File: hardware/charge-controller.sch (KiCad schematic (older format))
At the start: 47 parts, among them J1 Conn_02x04_Odd_Even, J2 Conn_02x03_Odd_Even, J4 CAN_TERM, Q1 MMBT3904, Q2 NCV8402xST, Q3 NCV8402xST, Q4 NCV8402xST, Q5 NCV8402xST, U1 Pico, U2 MCP2515-xST, U3 SN65HVD230, U4 TPS62160DGK

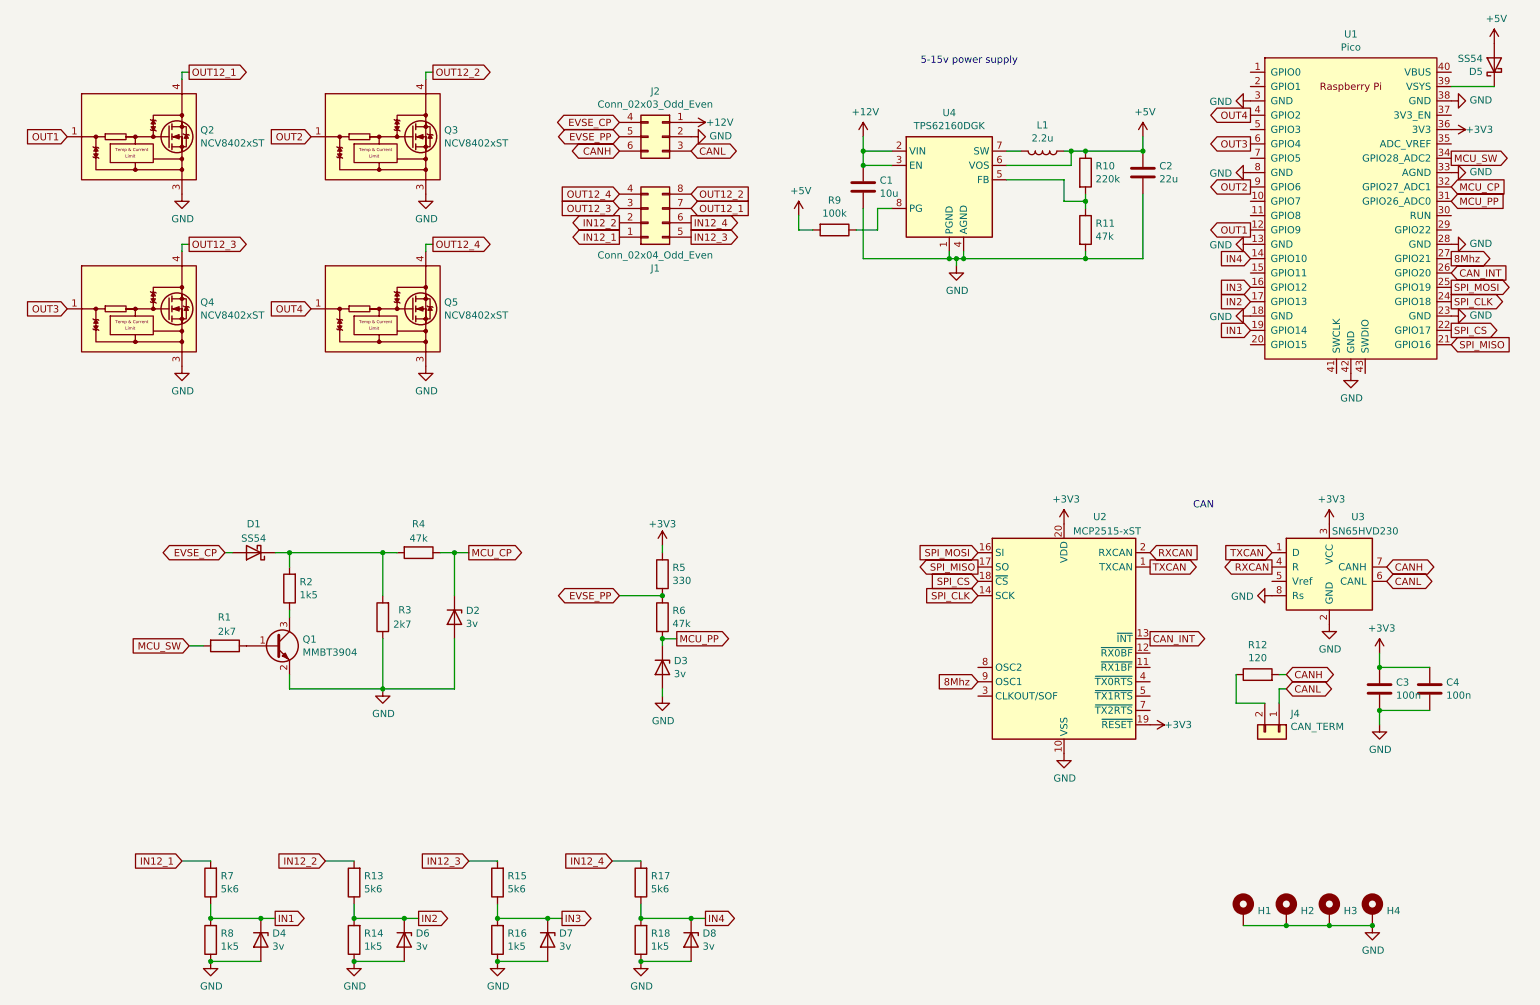
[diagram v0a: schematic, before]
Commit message: improve 12v inputs, connect CAN line driver sleep pin
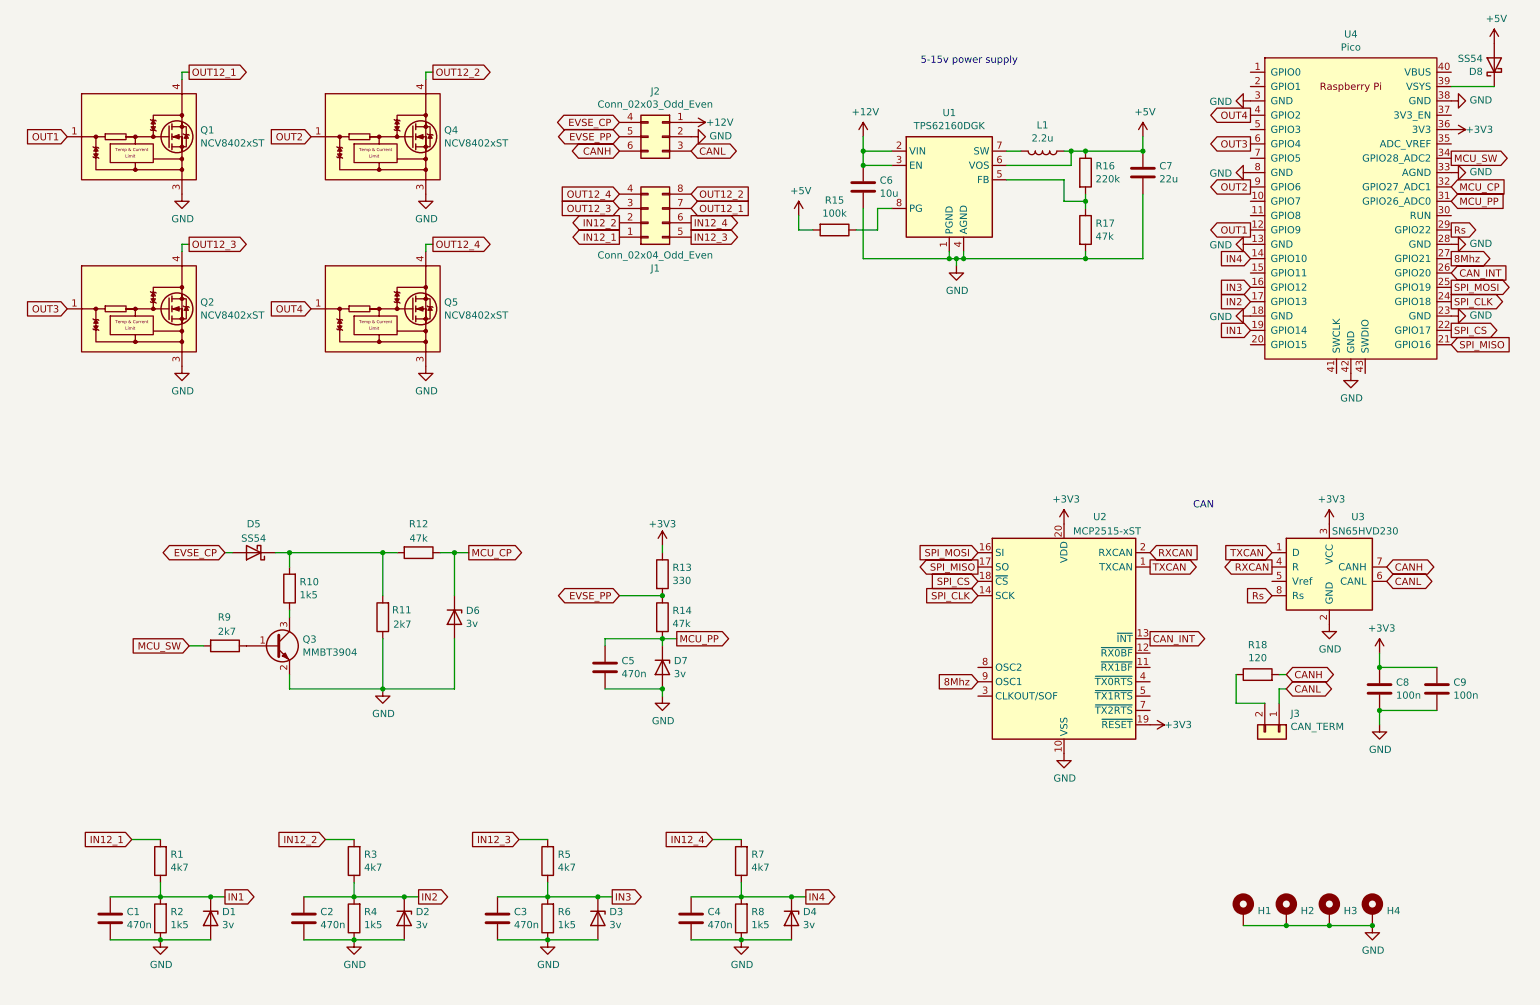
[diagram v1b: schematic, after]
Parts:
- added C1, C2, C3, C4, C5: 470n, Capacitor_SMD:C_0603_1608Metric, symbol Device:C
- R1: renamed from R7; value 5k6 -> 4k7; LCSC C23189 -> C23162
- R3: renamed from R13; value 5k6 -> 4k7; LCSC C23189 -> C23162
- R5: renamed from R15; value 5k6 -> 4k7; LCSC C23189 -> C23162
- R7: renamed from R17; value 5k6 -> 4k7; LCSC C23189 -> C23162
- renumbered C1 to C6, C2 to C7, C3 to C8, C4 to C9, D4 to D1, D6 to D2, D7 to D3, D8 to D4, D1 to D5, D2 to D6, D3 to D7, D5 to D8, J4 to J3, Q2 to Q1, Q4 to Q2, Q1 to Q3, Q3 to Q4, R2 to R10, R3 to R11, R4 to R12, R5 to R13, R6 to R14, R9 to R15, R10 to R16, R11 to R17, R12 to R18, R8 to R2, R14 to R4, R16 to R6, R18 to R8, R1 to R9, U4 to U1, U1 to U4
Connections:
- net GND: now also C1.2, C2.2, C3.2, C4.2, C5.2; no longer U3.8 (Rs)
- net IN1: now also C1.1
- net IN2: now also C2.1
- net IN3: now also C3.1
- net IN4: now also C4.1
- net MCU_PP: now also C5.1
- net Rs: now reaches U4.29 (GPIO22)
- net Rs: now also U3.8 (Rs)
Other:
- moved on the sheet: C9, D1, D2, D3, D4, R1, R2, R3, R4, R5, R6, R7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

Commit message: v3
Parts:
- renumbered J2 to J1, J1 to J2
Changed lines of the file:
@@
 CAN
 $Comp
-L Connector_Generic:Conn_02x03_Top_Bottom J2
+L Connector_Generic:Conn_02x03_Top_Bottom J1
 U 1 1 61C657A9
 P 5100 1450
-F 0 "J2" H 5150 1767 50  0000 C CNN
+F 0 "J1" H 5150 1767 50  0000 C CNN
 F 1 "Conn_02x03_Odd_Even" H 5150 1676 50  0000 C CNN
 F 2 "Connector_Molex:Molex_Micro-Fit_3.0_43045-0600_2x03_P3.00mm_Horizontal" H 5100 1450 50  0001 C CNN
@@
 IN1
 $Comp
-L Connector_Generic:Conn_02x04_Top_Bottom J1
+L Connector_Generic:Conn_02x04_Top_Bottom J2
 U 1 1 61C6623C
 P 5000 2050
-F 0 "J1" H 5050 2367 50  0000 C CNN
+F 0 "J2" H 5050 2367 50  0000 C CNN
 F 1 "Conn_02x04_Odd_Even" H 5050 2276 50  0000 C CNN
 F 2 "Connector_Molex:Molex_Micro-Fit_3.0_43045-0800_2x04_P3.00mm_Horizontal" H 5000 2050 50  0001 C CNN

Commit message: update schematic and picture
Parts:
- C1, C2, C3, C4, C5: value 470n -> 1u; LCSC C1623 -> C15849
- C7: LCSC C12891 -> C5672
- L1: footprint footprints:1227ASH100MP2 -> Inductor_SMD:L_Neosid_SMS-ME3015; LCSC C435389 -> C43389
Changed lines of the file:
@@
 F 0 "L1" V 7569 1550 50  0000 C CNN
 F 1 "2.2u" V 7660 1550 50  0000 C CNN
-F 2 "footprints:1227ASH100MP2" H 7750 1550 50  0001 C CNN
+F 2 "Inductor_SMD:L_Neosid_SMS-ME3015" H 7750 1550 50  0001 C CNN
 F 3 "~" H 7750 1550 50  0001 C CNN
-F 4 "C435389" V 7750 1550 50  0001 C CNN "LCSC"
+F 4 "C43389" V 7750 1550 50  0001 C CNN "LCSC"
 	1    7750 1550
 	0    1    1    0
@@
 F 2 "Capacitor_SMD:C_1206_3216Metric" H 8488 1550 50  0001 C CNN
 F 3 "~" H 8450 1700 50  0001 C CNN
-F 4 "C12891" H 8450 1700 50  0001 C CNN "LCSC"
+F 4 "C5672" H 8450 1700 50  0001 C CNN "LCSC"
 	1    8450 1700
 	1    0    0    -1
@@
 P 2600 6900
 F 0 "C2" H 2715 6946 50  0000 L CNN
-F 1 "470n" H 2715 6855 50  0000 L CNN
+F 1 "1u" H 2715 6855 50  0000 L CNN
 F 2 "Capacitor_SMD:C_0603_1608Metric" H 2638 6750 50  0001 C CNN
 F 3 "~" H 2600 6900 50  0001 C CNN
-F 4 "C1623" H 2600 6900 50  0001 C CNN "LCSC"
+F 4 "C15849" H 2600 6900 50  0001 C CNN "LCSC"
 	1    2600 6900
 	1    0    0    -1
@@
 P 3950 6900
 F 0 "C3" H 4065 6946 50  0000 L CNN
-F 1 "470n" H 4065 6855 50  0000 L CNN
+F 1 "1u" H 4065 6855 50  0000 L CNN
 F 2 "Capacitor_SMD:C_0603_1608Metric" H 3988 6750 50  0001 C CNN
 F 3 "~" H 3950 6900 50  0001 C CNN
-F 4 "C1623" H 3950 6900 50  0001 C CNN "LCSC"
+F 4 "C15849" H 3950 6900 50  0001 C CNN "LCSC"
 	1    3950 6900
 	1    0    0    -1
@@
 P 5300 6900
 F 0 "C4" H 5415 6946 50  0000 L CNN
-F 1 "470n" H 5415 6855 50  0000 L CNN
+F 1 "1u" H 5415 6855 50  0000 L CNN
 F 2 "Capacitor_SMD:C_0603_1608Metric" H 5338 6750 50  0001 C CNN
 F 3 "~" H 5300 6900 50  0001 C CNN
-F 4 "C1623" H 5300 6900 50  0001 C CNN "LCSC"
+F 4 "C15849" H 5300 6900 50  0001 C CNN "LCSC"
 	1    5300 6900
 	1    0    0    -1
@@
 P 1250 6900
 F 0 "C1" H 1365 6946 50  0000 L CNN
-F 1 "470n" H 1365 6855 50  0000 L CNN
+F 1 "1u" H 1365 6855 50  0000 L CNN
 F 2 "Capacitor_SMD:C_0603_1608Metric" H 1288 6750 50  0001 C CNN
 F 3 "~" H 1250 6900 50  0001 C CNN
-F 4 "C1623" H 1250 6900 50  0001 C CNN "LCSC"
+F 4 "C15849" H 1250 6900 50  0001 C CNN "LCSC"
 	1    1250 6900
 	1    0    0    -1
@@
 P 4700 5150
 F 0 "C5" H 4815 5196 50  0000 L CNN
-F 1 "470n" H 4815 5105 50  0000 L CNN
+F 1 "1u" H 4815 5105 50  0000 L CNN
 F 2 "Capacitor_SMD:C_0603_1608Metric" H 4738 5000 50  0001 C CNN
 F 3 "~" H 4700 5150 50  0001 C CNN
-F 4 "C1623" H 4700 5150 50  0001 C CNN "LCSC"
+F 4 "C15849" H 4700 5150 50  0001 C CNN "LCSC"
 	1    4700 5150
 	1    0    0    -1

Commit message: rework inuts
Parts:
- removed D6, D7: 3v, Diode_SMD:D_MiniMELF, symbol Device:D_Zener
- removed R12, R14: 47k, Resistor_SMD:R_0603_1608Metric, symbol Device:R
- added Q6: MMBT3904, Package_TO_SOT_SMD:SOT-23, symbol Transistor_BJT:MMBT3904
- C1, C2, C3, C4: value 1u -> 100n; LCSC C15849 -> C14663
- D1, D2, D3, D4: value 3v -> 3.3v
- R1, R3, R5, R7: value 4k7 -> 47k; LCSC C23162 -> C25819
- R2, R4, R6, R8: value 1k5 -> 4.7k; LCSC C22843 -> C23162
- R9: value 2k7 -> 1k5; LCSC C13167 -> C22843
- renumbered D8 to D6, J2 to J1, J1 to J2, Q4 to Q2, Q2 to Q3, Q5 to Q4, Q3 to Q5, R13 to R12, R15 to R13, R16 to R14, R17 to R15, R18 to R16, U4 to U2, U2 to U3, U3 to U4
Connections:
- net MCU_PP is gone; now on net EVSE_PP: C5.1, U2.31 (GPIO26_ADC0)
- net GND: now also R1.2, R3.2, R5.2, R7.2, Q6.2 (E); no longer R11.1, R2.1, R4.1, R6.1, R8.1
- net IN1: no longer R1.1
- net IN12_1: now also R1.1, R2.1; no longer R1.2
- net IN12_2: now also R3.1, R4.1; no longer R3.2
- net IN12_3: now also R5.1, R6.1; no longer R5.2
- net IN12_4: now also R7.1, R8.1; no longer R7.2
- net IN2: no longer R3.1
- net IN3: no longer R5.1
- net IN4: no longer R7.1
- net MCU_CP: now also Q6.3 (C)
- net MCU_SW: now also R9.1; no longer R9.2
- net at D5.1 (K), R10.2: now also R11.1; no longer R11.2
- net at Q5.1 (B): now also R9.2; no longer R9.1
- new net: Q6.1 (B), R11.2
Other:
- moved on the sheet: C5, C8, C9, D5, H1, H2, H3, H4, J3, Q1, Q2, Q3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

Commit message: finish inputs
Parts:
- C5: value 1u -> 100n; LCSC C15849 -> C14663
- R2, R4, R6, R8: value 4.7k -> 5.6k; LCSC C23162 -> C23189
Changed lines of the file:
@@
 P 6100 4750
 F 0 "C5" H 6215 4796 50  0000 L CNN
-F 1 "1u" H 6215 4705 50  0000 L CNN
+F 1 "100n" H 6215 4705 50  0000 L CNN
 F 2 "Capacitor_SMD:C_0603_1608Metric" H 6138 4600 50  0001 C CNN
 F 3 "~" H 6100 4750 50  0001 C CNN
-F 4 "C15849" H 6100 4750 50  0001 C CNN "LCSC"
+F 4 "C14663" H 6100 4750 50  0001 C CNN "LCSC"
 	1    6100 4750
 	1    0    0    -1
@@
 P 4450 6700
 F 0 "R6" H 4520 6746 50  0000 L CNN
-F 1 "4.7k" H 4520 6655 50  0000 L CNN
+F 1 "5.6k" H 4520 6655 50  0000 L CNN
 F 2 "Resistor_SMD:R_0603_1608Metric" V 4380 6700 50  0001 C CNN
 F 3 "~" H 4450 6700 50  0001 C CNN
-F 4 "C23162" H 4450 6700 50  0001 C CNN "LCSC"
+F 4 "C23189" H 4450 6700 50  0001 C CNN "LCSC"
 	1    4450 6700
 	1    0    0    -1
@@
 P 5950 6700
 F 0 "R8" H 6020 6746 50  0000 L CNN
-F 1 "4.7k" H 6020 6655 50  0000 L CNN
+F 1 "5.6k" H 6020 6655 50  0000 L CNN
 F 2 "Resistor_SMD:R_0603_1608Metric" V 5880 6700 50  0001 C CNN
 F 3 "~" H 5950 6700 50  0001 C CNN
-F 4 "C23162" H 5950 6700 50  0001 C CNN "LCSC"
+F 4 "C23189" H 5950 6700 50  0001 C CNN "LCSC"
 	1    5950 6700
 	1    0    0    -1
@@
 P 2950 6700
 F 0 "R4" H 3020 6746 50  0000 L CNN
-F 1 "4.7k" H 3020 6655 50  0000 L CNN
+F 1 "5.6k" H 3020 6655 50  0000 L CNN
 F 2 "Resistor_SMD:R_0603_1608Metric" V 2880 6700 50  0001 C CNN
 F 3 "~" H 2950 6700 50  0001 C CNN
-F 4 "C23162" H 2950 6700 50  0001 C CNN "LCSC"
+F 4 "C23189" H 2950 6700 50  0001 C CNN "LCSC"
 	1    2950 6700
 	1    0    0    -1
@@
 P 1450 6700
 F 0 "R2" H 1520 6746 50  0000 L CNN
-F 1 "4.7k" H 1520 6655 50  0000 L CNN
+F 1 "5.6k" H 1520 6655 50  0000 L CNN
 F 2 "Resistor_SMD:R_0603_1608Metric" V 1380 6700 50  0001 C CNN
 F 3 "~" H 1450 6700 50  0001 C CNN
-F 4 "C23162" H 1450 6700 50  0001 C CNN "LCSC"
+F 4 "C23189" H 1450 6700 50  0001 C CNN "LCSC"
 	1    1450 6700
 	1    0    0    -1

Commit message: begin EVSE comms
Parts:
- U4: value SN65HVD230 -> SN65HVD231; LCSC C12084 -> C129257
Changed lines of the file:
@@
 P 10000 4400
 F 0 "U4" H 10200 4750 50  0000 C CNN
-F 1 "SN65HVD230" H 10250 4650 50  0000 C CNN
+F 1 "SN65HVD231" H 10250 4650 50  0000 C CNN
 F 2 "Package_SO:SOIC-8_3.9x4.9mm_P1.27mm" H 10000 3900 50  0001 C CNN
 F 3 "http://www.ti.com/lit/ds/symlink/sn65hvd230.pdf" H 9900 4800 50  0001 C CNN
-F 4 "C12084" H 10000 4400 50  0001 C CNN "LCSC"
+F 4 "C129257" H 10000 4400 50  0001 C CNN "LCSC"
 	1    10000 4400
 	1    0    0    -1
